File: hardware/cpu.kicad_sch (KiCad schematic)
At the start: 62 parts, among them Q5 MMBT3904, U1 H3, Y1 32kHz, Y3 24MHz

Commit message: Improve heat dissipation and layout
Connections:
- net GND: now also U1.A10 (PE1), U1.A11 (PE11), U1.B10 (PE0), U1.B11 (PE2), U1.C10 (PE3), U1.C11 (PE8), U1.C8 (PE7), U1.C9 (PE4), U1.D10 (PE6), U1.E10 (PE5), U1.E8 (PE10)
- net DQ16: no longer names the net of U1.Y17 (SDQ16)
- net DQ17: no longer names the net of U1.AA17 (SDQ17)
- net DQ18: no longer names the net of U1.Y16 (SDQ18)
- net DQ19: no longer names the net of U1.W15 (SDQ19)
- net DQ20: no longer names the net of U1.Y14 (SDQ20)
- net DQ21: no longer names the net of U1.AA14 (SDQ21)
- net DQ22: no longer names the net of U1.Y13 (SDQ22)
- net DQ23: no longer names the net of U1.Y12 (SDQ23)
- net DQ24: no longer names the net of U1.W12 (SDQ24)
- net DQ25: no longer names the net of U1.AA11 (SDQ25)
- net DQ26: no longer names the net of U1.Y11 (SDQ26)
- net DQ27: no longer names the net of U1.Y10 (SDQ27)
- net DQ28: no longer names the net of U1.W9 (SDQ28)
- net DQ29: no longer names the net of U1.AA8 (SDQ29)
- net DQ30: no longer names the net of U1.Y8 (SDQ30)
- net DQ31: no longer names the net of U1.Y7 (SDQ31)
- net DQM2: no longer names the net of U1.AA18 (SDQM2)
- net DQM3: no longer names the net of U1.AA12 (SDQM3)
- net DQS2+: no longer names the net of U1.AA15 (SDQS2)
- net DQS2-: no longer names the net of U1.Y15 (SDQS2B)
- net DQS3+: no longer names the net of U1.AA9 (SDQS3)
- net DQS3-: no longer names the net of U1.Y9 (SDQS3B)
- no-connect marks 42 -> 72
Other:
- note added: "GND for heat dissipation"

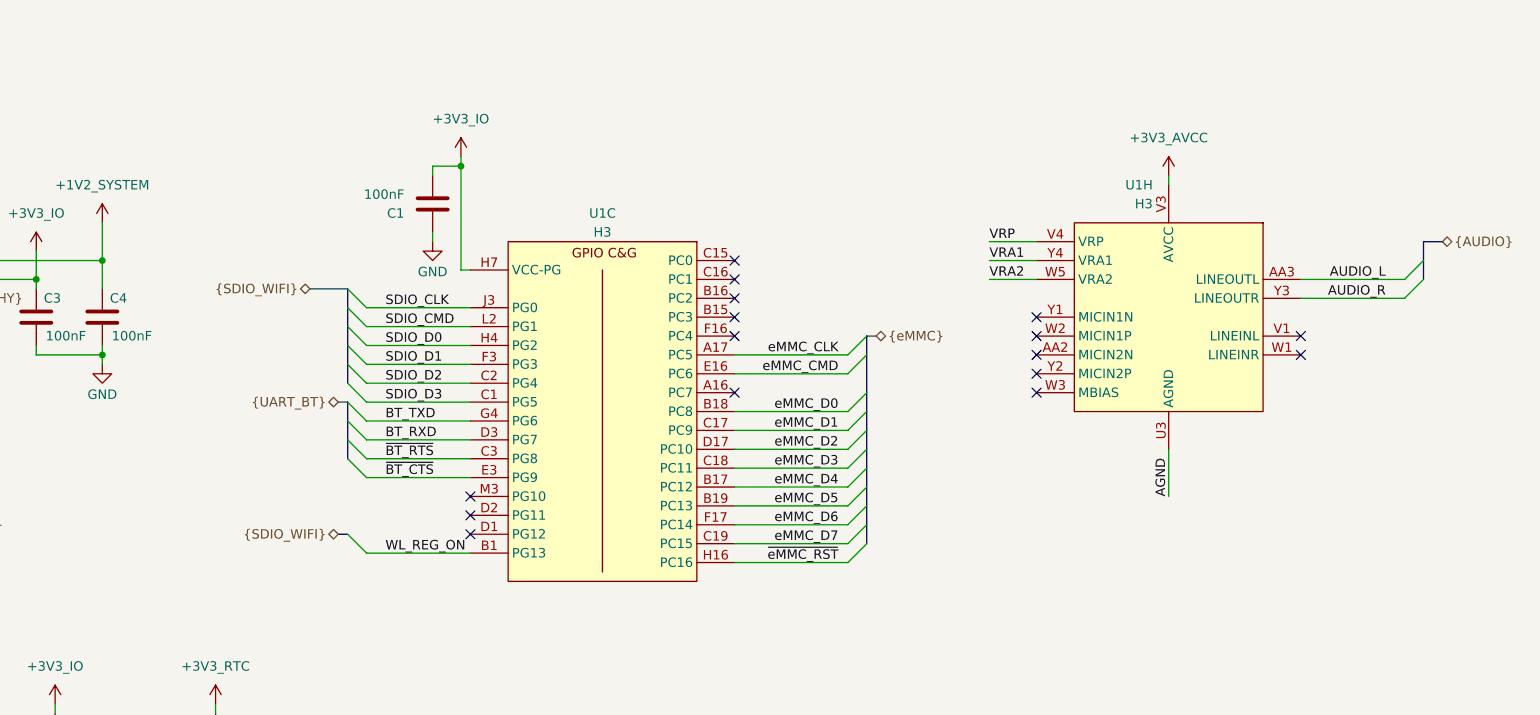
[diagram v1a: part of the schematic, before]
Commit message: Add some more decoupling and move trace
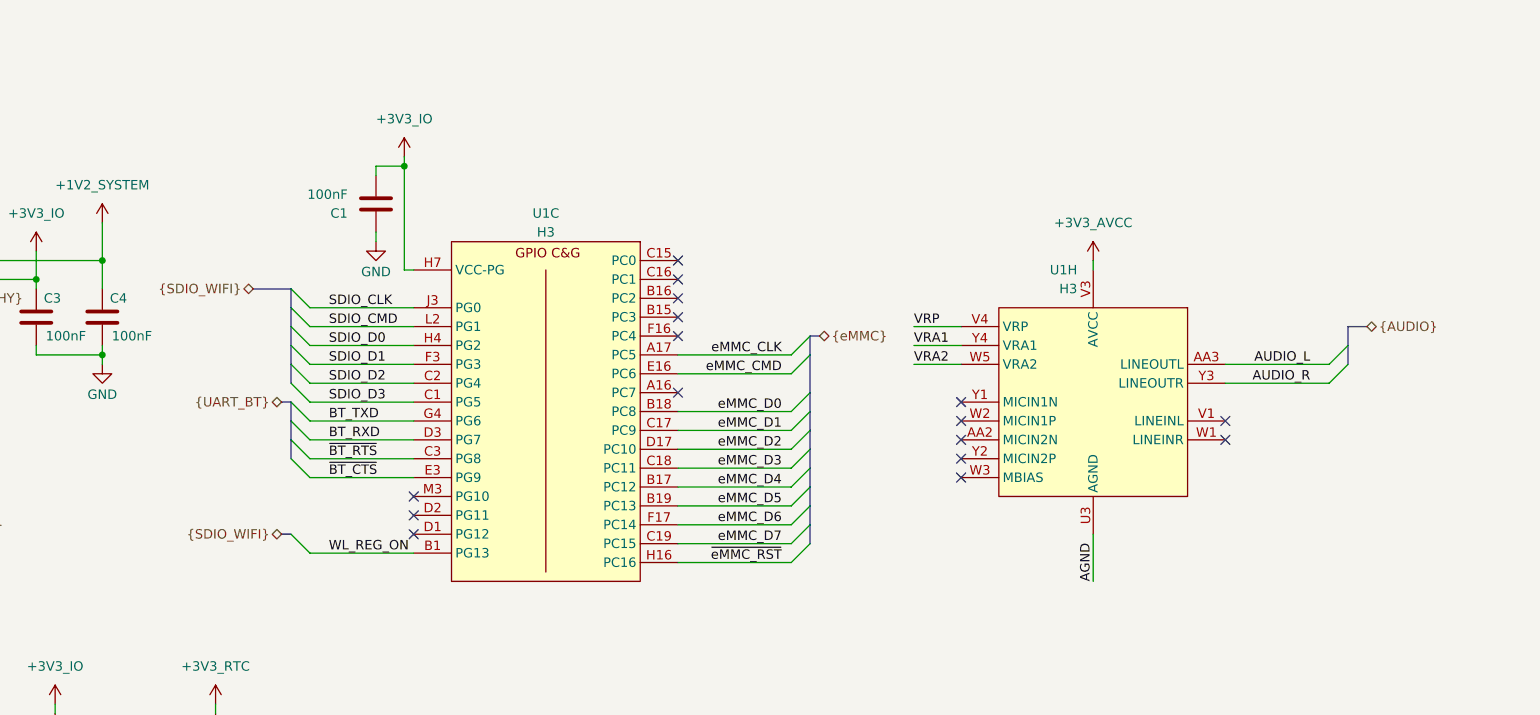
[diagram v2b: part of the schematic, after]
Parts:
- Y3: LCSC Part # C362340 -> C37635323
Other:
- moved on the sheet: C1, U1C, U1H
